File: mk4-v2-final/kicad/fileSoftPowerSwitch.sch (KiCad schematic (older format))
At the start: 11 parts, among them Q20 Q_NMOS_GDS, Q21 2N3904, Q22 2N3904

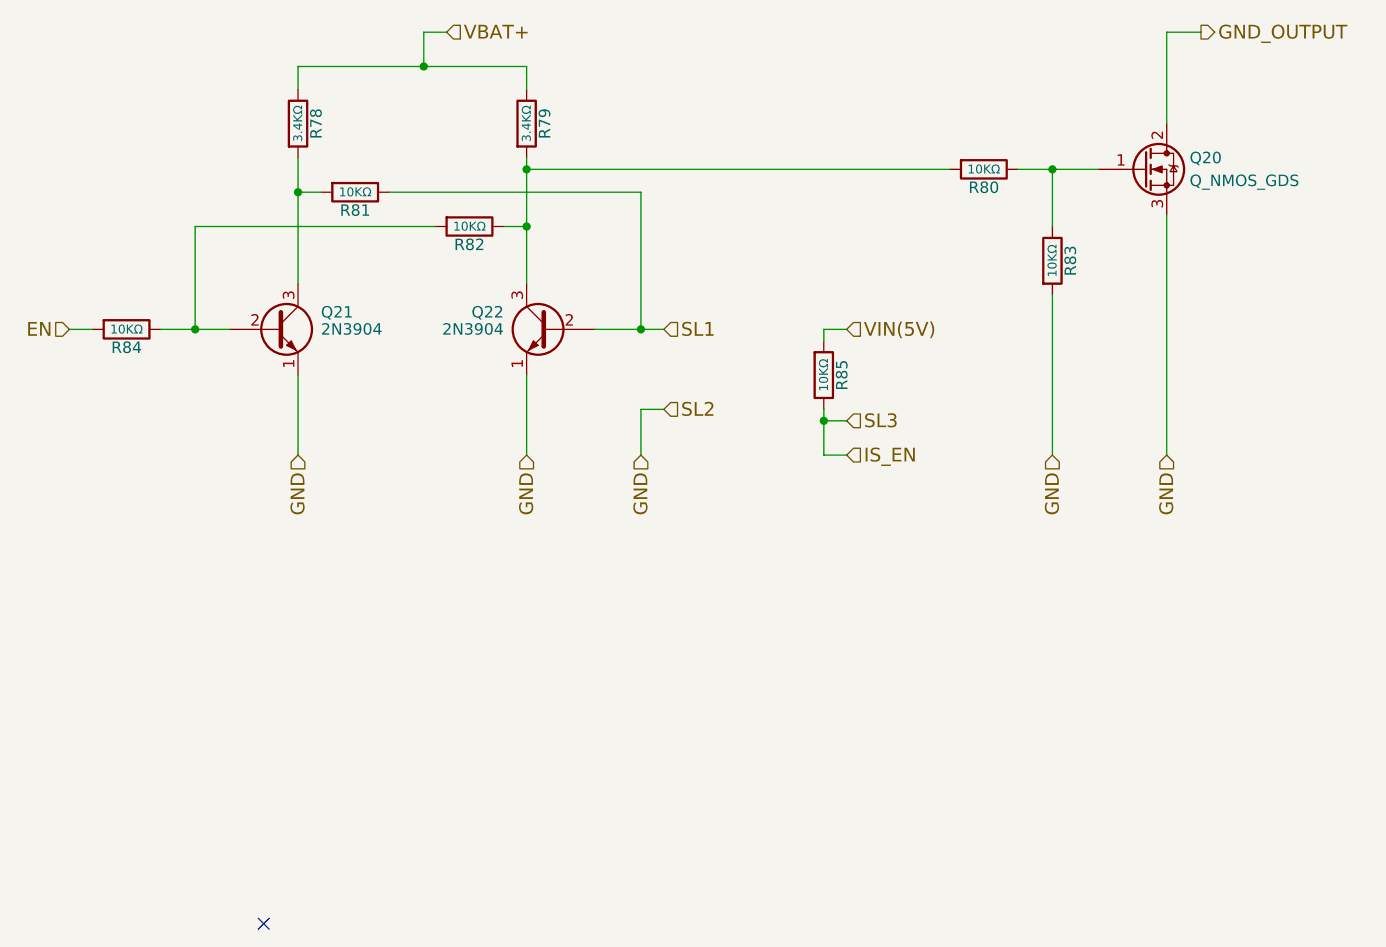
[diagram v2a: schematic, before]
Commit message: schematic is done, footprint association and netlist are also done
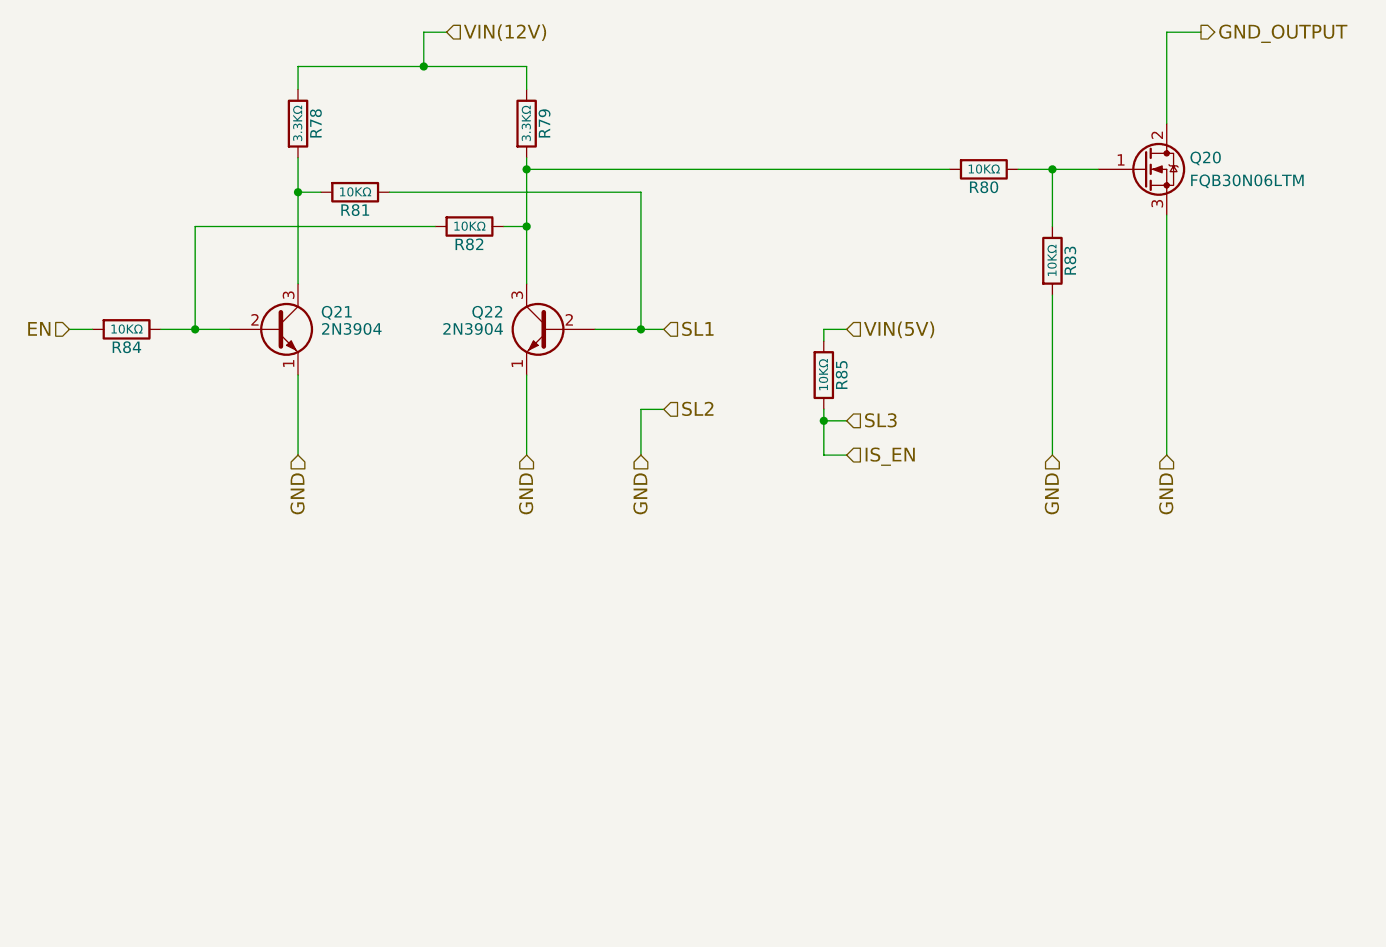
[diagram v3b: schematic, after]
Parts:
- Q20: value Q_NMOS_GDS -> FQB30N06LTM; footprint TO_SOT_Packages_THT:TO-220-3_Vertical -> TO_SOT_Packages_SMD:TO-263-3_TabPin2; digikey-pn (none) -> FQB30N06LTMCT-ND; mfg-pn (none) -> FQB30N06LTM
- Q21, Q22: digikey-pn (none) -> 2N3904FS-ND; mfg-pn (none) -> 2N3904BU
- R78, R79: value 3.4KΩ -> 3.3KΩ; footprint Resistors_THT:R_Axial_DIN0207_L6.3mm_D2.5mm_P10.16mm_Horizontal -> Resistors_THT:R_Axial_DIN0204_L3.6mm_D1.6mm_P5.08mm_Horizontal; digikey-pn (none) -> BC3499CT-ND; mfg-pn (none) -> MBA02040C3301FRP00
- R80, R81, R82, R83, R84, R85: footprint Resistors_THT:R_Axial_DIN0207_L6.3mm_D2.5mm_P10.16mm_Horizontal -> Resistors_THT:R_Axial_DIN0204_L3.6mm_D1.6mm_P5.08mm_Horizontal; digikey-pn (none) -> BC10.0KXCT-ND; mfg-pn (none) -> MBA02040C1002FRP00
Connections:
- net VBAT+ renamed VIN(12V)
- no-connect marks 1 -> 0
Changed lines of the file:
@@
 EESchema Schematic File Version 2
-LIBS:hitchco-mk4-rescue
 LIBS:power
 LIBS:device
@@
 LIBS:cd4013b
 LIBS:ncs3s1205sc
+LIBS:lca715
+LIBS:SN74HC595N
+LIBS:CD74HC4067
 LIBS:hitchco-mk4-cache
 EELAYER 25 0
@@
 $Descr A4 11693 8268
 encoding utf-8
-Sheet 44 54
+Sheet 40 54
 Title ""
 Date ""
@@
 P 4400 2750
 F 0 "R78" V 4480 2750 50  0000 C CNN
-F 1 "3.4KΩ" V 4400 2750 39  0000 C CNN
-F 2 "Resistors_THT:R_Axial_DIN0207_L6.3mm_D2.5mm_P10.16mm_Horizontal" V 4330 2750 50  0001 C CNN
+F 1 "3.3KΩ" V 4400 2750 39  0000 C CNN
+F 2 "Resistors_THT:R_Axial_DIN0204_L3.6mm_D1.6mm_P5.08mm_Horizontal" V 4330 2750 50  0001 C CNN
 F 3 "" H 4400 2750 50  0001 C CNN
+F 4 "BC3499CT-ND" H 4480 2850 50  0001 C CNN "digikey-pn"
+F 5 "MBA02040C3301FRP00" H 4480 2850 50  0001 C CNN "mfg-pn"
 	1    4400 2750
 	1    0    0    -1
@@
 F 0 "R81" V 4730 3050 50  0000 C CNN
 F 1 "10KΩ" V 4650 3050 39  0000 C CNN
-F 2 "Resistors_THT:R_Axial_DIN0207_L6.3mm_D2.5mm_P10.16mm_Horizontal" V 4580 3050 50  0001 C CNN
+F 2 "Resistors_THT:R_Axial_DIN0204_L3.6mm_D1.6mm_P5.08mm_Horizontal" V 4580 3050 50  0001 C CNN
 F 3 "" H 4650 3050 50  0001 C CNN
+F 4 "BC10.0KXCT-ND" H 4730 3150 50  0001 C CNN "digikey-pn"
+F 5 "MBA02040C1002FRP00" H 4730 3150 50  0001 C CNN "mfg-pn"
 	1    4650 3050
 	0    1    1    0
@@
 F 1 "2N3904" H 4500 3650 50  0000 L CNN
 F 2 "TO_SOT_Packages_THT:TO-92_Molded_Narrow" H 4500 3575 50  0001 L CIN
-F 3 "" H 4300 3650 50  0001 L CNN
+F 3 "https://www.fairchildsemi.com/datasheets/MM/MMBT3904.pdf" H 4300 3650 50  0001 L CNN
+F 4 "2N3904FS-ND" H 4500 3825 50  0001 C CNN "digikey-pn"
+F 5 "2N3904BU" H 4500 3825 50  0001 C CNN "mfg-pn"
 	1    4300 3650
 	1    0    0    -1
@@
 F 0 "R82" V 5230 3200 50  0000 C CNN
 F 1 "10KΩ" V 5150 3200 39  0000 C CNN
-F 2 "Resistors_THT:R_Axial_DIN0207_L6.3mm_D2.5mm_P10.16mm_Horizontal" V 5080 3200 50  0001 C CNN
+F 2 "Resistors_THT:R_Axial_DIN0204_L3.6mm_D1.6mm_P5.08mm_Horizontal" V 5080 3200 50  0001 C CNN
 F 3 "" H 5150 3200 50  0001 C CNN
+F 4 "BC10.0KXCT-ND" H 5230 3300 50  0001 C CNN "digikey-pn"
+F 5 "MBA02040C1002FRP00" H 5230 3300 50  0001 C CNN "mfg-pn"
 	1    5150 3200
 	0    1    1    0
@@
 P 5400 2750
 F 0 "R79" V 5480 2750 50  0000 C CNN
-F 1 "3.4KΩ" V 5400 2750 39  0000 C CNN
-F 2 "Resistors_THT:R_Axial_DIN0207_L6.3mm_D2.5mm_P10.16mm_Horizontal" V 5330 2750 50  0001 C CNN
+F 1 "3.3KΩ" V 5400 2750 39  0000 C CNN
+F 2 "Resistors_THT:R_Axial_DIN0204_L3.6mm_D1.6mm_P5.08mm_Horizontal" V 5330 2750 50  0001 C CNN
 F 3 "" H 5400 2750 50  0001 C CNN
+F 4 "BC3499CT-ND" H 5480 2850 50  0001 C CNN "digikey-pn"
+F 5 "MBA02040C3301FRP00" H 5480 2850 50  0001 C CNN "mfg-pn"
 	1    5400 2750
 	1    0    0    -1
@@
 F 1 "2N3904" H 5700 3650 50  0000 L CNN
 F 2 "TO_SOT_Packages_THT:TO-92_Molded_Narrow" H 5700 3575 50  0001 L CIN
-F 3 "" H 5500 3650 50  0001 L CNN
+F 3 "https://www.fairchildsemi.com/datasheets/MM/MMBT3904.pdf" H 5500 3650 50  0001 L CNN
+F 4 "2N3904FS-ND" H 5700 3825 50  0001 C CNN "digikey-pn"
+F 5 "2N3904BU" H 5700 3825 50  0001 C CNN "mfg-pn"
 	1    5500 3650
 	-1   0    0    -1
 $EndComp
-Text HLabel 5400 4200 3    60   Input ~ 0
-GND
-Text HLabel 4400 4200 3    60   Input ~ 0
-GND
-Text HLabel 5050 2350 2    60   Input ~ 0
-VBAT+
 $Comp
 L R R80
@@
 F 0 "R80" V 7480 2950 50  0000 C CNN
 F 1 "10KΩ" V 7400 2950 39  0000 C CNN
-F 2 "Resistors_THT:R_Axial_DIN0207_L6.3mm_D2.5mm_P10.16mm_Horizontal" V 7330 2950 50  0001 C CNN
+F 2 "Resistors_THT:R_Axial_DIN0204_L3.6mm_D1.6mm_P5.08mm_Horizontal" V 7330 2950 50  0001 C CNN
 F 3 "" H 7400 2950 50  0001 C CNN
+F 4 "BC10.0KXCT-ND" H 7480 3050 50  0001 C CNN "digikey-pn"
+F 5 "MBA02040C1002FRP00" H 7480 3050 50  0001 C CNN "mfg-pn"
 	1    7400 2950
 	0    1    1    0
@@
 F 0 "R83" V 7780 3350 50  0000 C CNN
 F 1 "10KΩ" V 7700 3350 39  0000 C CNN
-F 2 "Resistors_THT:R_Axial_DIN0207_L6.3mm_D2.5mm_P10.16mm_Horizontal" V 7630 3350 50  0001 C CNN
+F 2 "Resistors_THT:R_Axial_DIN0204_L3.6mm_D1.6mm_P5.08mm_Horizontal" V 7630 3350 50  0001 C CNN
 F 3 "" H 7700 3350 50  0001 C CNN
+F 4 "BC10.0KXCT-ND" H 7780 3450 50  0001 C CNN "digikey-pn"
+F 5 "MBA02040C1002FRP00" H 7780 3450 50  0001 C CNN "mfg-pn"
 	1    7700 3350
 	1    0    0    -1
 $EndComp
+$Comp
+L R R85
+U 1 1 5A25E32E
+P 6700 3850
+F 0 "R85" V 6780 3850 50  0000 C CNN
+F 1 "10KΩ" V 6700 3850 39  0000 C CNN
+F 2 "Resistors_THT:R_Axial_DIN0204_L3.6mm_D1.6mm_P5.08mm_Horizontal" V 6630 3850 50  0001 C CNN
+F 3 "" H 6700 3850 50  0001 C CNN
+F 4 "BC10.0KXCT-ND" H 6780 3950 50  0001 C CNN "digikey-pn"
+F 5 "MBA02040C1002FRP00" H 6780 3950 50  0001 C CNN "mfg-pn"
+	1    6700 3850
+	1    0    0    1
+$EndComp
+$Comp
+L R R84
+U 1 1 5A25E339
+P 3650 3650
+F 0 "R84" V 3730 3650 50  0000 C CNN
+F 1 "10KΩ" V 3650 3650 39  0000 C CNN
+F 2 "Resistors_THT:R_Axial_DIN0204_L3.6mm_D1.6mm_P5.08mm_Horizontal" V 3580 3650 50  0001 C CNN
+F 3 "" H 3650 3650 50  0001 C CNN
+F 4 "BC10.0KXCT-ND" H 3730 3750 50  0001 C CNN "digikey-pn"
+F 5 "MBA02040C1002FRP00" H 3730 3750 50  0001 C CNN "mfg-pn"
+	1    3650 3650
+	0    1    1    0
+$EndComp
+$Comp
+L Q_NMOS_GDS Q20
+U 1 1 5A2EEE12
+P 8100 2950
+F 0 "Q20" H 8300 3000 50  0000 L CNN
+F 1 "FQB30N06LTM" H 8300 2900 50  0000 L CNN
+F 2 "TO_SOT_Packages_SMD:TO-263-3_TabPin2" H 8300 3050 50  0001 C CNN
+F 3 "http://www.onsemi.com/pub/Collateral/NTB5605P-D.PDF" H 8100 2950 50  0001 C CNN
+F 4 "FQB30N06LTMCT-ND" H 8300 3100 50  0001 C CNN "digikey-pn"
+F 5 "FQB30N06LTM" H 8300 3100 50  0001 C CNN "mfg-pn"
+	1    8100 2950
+	1    0    0    -1
+$EndComp
+Text HLabel 5400 4200 3    60   Input ~ 0
+GND
+Text HLabel 4400 4200 3    60   Input ~ 0
+GND
 Text HLabel 7700 4200 3    60   Input ~ 0
 GND
@@
 Text HLabel 6800 4050 2    60   Input ~ 0
 SL3
-$Comp
-L R R85
-U 1 1 5A25E32E
-P 6700 3850
-F 0 "R85" V 6780 3850 50  0000 C CNN
-F 1 "10KΩ" V 6700 3850 39  0000 C CNN
-F 2 "Resistors_THT:R_Axial_DIN0207_L6.3mm_D2.5mm_P10.16mm_Horizontal" V 6630 3850 50  0001 C CNN
-F 3 "" H 6700 3850 50  0001 C CNN
-	1    6700 3850
-	1    0    0    1
-$EndComp
 Text HLabel 6800 3650 2    60   Input ~ 0
 VIN(5V)
-$Comp
-L R R84
-U 1 1 5A25E339
-P 3650 3650
-F 0 "R84" V 3730 3650 50  0000 C CNN
-F 1 "10KΩ" V 3650 3650 39  0000 C CNN
-F 2 "Resistors_THT:R_Axial_DIN0207_L6.3mm_D2.5mm_P10.16mm_Horizontal" V 3580 3650 50  0001 C CNN
-F 3 "" H 3650 3650 50  0001 C CNN
-	1    3650 3650
-	0    1    1    0
-$EndComp
-Wire Wire Line
-	4400 2900 4400 3450
-Wire Wire Line
-	5400 2900 5400 3450
-Wire Wire Line
-	3950 3200 3950 3650
-Connection ~ 5400 3200
-Wire Wire Line
-	5000 3200 3950 3200
-Wire Wire Line
-	5300 3200 5400 3200
-Wire Wire Line
-	5400 3850 5400 4200
-Wire Wire Line
-	4400 3850 4400 4200
-Connection ~ 3950 3650
-Wire Wire Line
-	4400 2600 4400 2500
-Wire Wire Line
-	4400 2500 5400 2500
-Wire Wire Line
-	4950 2350 4950 2500
-Wire Wire Line
-	5400 2500 5400 2600
-Connection ~ 4950 2500
-Wire Wire Line
-	5400 2950 7250 2950
-Connection ~ 5400 2950
-Wire Wire Line
-	7700 3200 7700 2950
-Wire Wire Line
-	7700 3500 7700 4200
-Wire Wire Line
-	8200 3150 8200 4200
-Wire Wire Line
-	8200 2350 8200 2750
-Wire Wire Line
-	5700 3650 6000 3650
-Connection ~ 5900 3650
-Connection ~ 4400 3050
-Wire Wire Line
-	4400 3050 4500 3050
-Wire Wire Line
-	4800 3050 5900 3050
-Connection ~ 7700 2950
-Wire Wire Line
-	5900 3050 5900 3650
-Wire Wire Line
-	6800 4050 6700 4050
-Wire Wire Line
-	6700 4000 6700 4200
-Wire Wire Line
-	6800 3650 6700 3650
-Wire Wire Line
-	6700 3650 6700 3700
-Wire Wire Line
-	6000 4000 5900 4000
-Wire Wire Line
-	5900 4000 5900 4200
-Wire Wire Line
-	6700 4200 6800 4200
-Connection ~ 6700 4050
-Wire Wire Line
-	7550 2950 7900 2950
-Wire Wire Line
-	8350 2350 8200 2350
-Wire Wire Line
-	4950 2350 5050 2350
 Text HLabel 6800 4200 2    60   Input ~ 0
 IS_EN
 Text HLabel 3400 3650 0    60   Input ~ 0
 EN
-NoConn ~ 4250 6250
-$Comp
-L Q_NMOS_GDS Q20
-U 1 1 5A2EEE12
-P 8100 2950
-F 0 "Q20" H 8300 3000 50  0000 L CNN
-F 1 "Q_NMOS_GDS" H 8300 2900 50  0000 L CNN
-F 2 "TO_SOT_Packages_THT:TO-220-3_Vertical" H 8300 3050 50  0001 C CNN
-F 3 "" H 8100 2950 50  0001 C CNN
-	1    8100 2950
-	1    0    0    -1
-$EndComp
+Text HLabel 5050 2350 2    60   Input ~ 0
+VIN(12V)
+Wire Wire Line
+	4400 2900 4400 3450
+Wire Wire Line
+	5400 2900 5400 3450
+Wire Wire Line
+	3950 3200 3950 3650
+Wire Wire Line
+	5000 3200 3950 3200
+Wire Wire Line
+	5300 3200 5400 3200
+Wire Wire Line
+	5400 3850 5400 4200
+Wire Wire Line
+	4400 3850 4400 4200
+Wire Wire Line
+	4400 2600 4400 2500
+Wire Wire Line
+	4400 2500 5400 2500
+Wire Wire Line
+	4950 2350 4950 2500
+Wire Wire Line
+	5400 2500 5400 2600
+Wire Wire Line
+	5400 2950 7250 2950
+Wire Wire Line
+	7700 3200 7700 2950
+Wire Wire Line
+	7700 3500 7700 4200
+Wire Wire Line
+	8200 3150 8200 4200
+Wire Wire Line
+	8200 2350 8200 2750
+Wire Wire Line
+	5700 3650 6000 3650
+Wire Wire Line
+	4400 3050 4500 3050
+Wire Wire Line
+	4800 3050 5900 3050
+Wire Wire Line
+	5900 3050 5900 3650
+Wire Wire Line
+	6800 4050 6700 4050
+Wire Wire Line
+	6700 4000 6700 4200
+Wire Wire Line
+	6800 3650 6700 3650
+Wire Wire Line
+	6700 3650 6700 3700
+Wire Wire Line
+	6000 4000 5900 4000
+Wire Wire Line
+	5900 4000 5900 4200
+Wire Wire Line
+	6700 4200 6800 4200
+Wire Wire Line
+	7550 2950 7900 2950
+Wire Wire Line
+	8350 2350 8200 2350
+Wire Wire Line
+	4950 2350 5050 2350
 Wire Wire Line
 	3400 3650 3500 3650
 Wire Wire Line
 	3800 3650 4100 3650
+Connection ~ 5400 3200
+Connection ~ 3950 3650
+Connection ~ 4950 2500
+Connection ~ 5400 2950
+Connection ~ 5900 3650
+Connection ~ 4400 3050
+Connection ~ 7700 2950
+Connection ~ 6700 4050
 $EndSCHEMATC

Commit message: all components on the board
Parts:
- Q21, Q22: footprint TO_SOT_Packages_THT:TO-92_Molded_Narrow -> TO_SOT_Packages_THT:TO-92_Inline_Narrow_Oval
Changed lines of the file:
@@
 F 0 "Q21" H 4500 3725 50  0000 L CNN
 F 1 "2N3904" H 4500 3650 50  0000 L CNN
-F 2 "TO_SOT_Packages_THT:TO-92_Molded_Narrow" H 4500 3575 50  0001 L CIN
+F 2 "TO_SOT_Packages_THT:TO-92_Inline_Narrow_Oval" H 4500 3575 50  0001 L CIN
 F 3 "https://www.fairchildsemi.com/datasheets/MM/MMBT3904.pdf" H 4300 3650 50  0001 L CNN
 F 4 "2N3904FS-ND" H 4500 3825 50  0001 C CNN "digikey-pn"
@@
 F 0 "Q22" H 5700 3725 50  0000 L CNN
 F 1 "2N3904" H 5700 3650 50  0000 L CNN
-F 2 "TO_SOT_Packages_THT:TO-92_Molded_Narrow" H 5700 3575 50  0001 L CIN
+F 2 "TO_SOT_Packages_THT:TO-92_Inline_Narrow_Oval" H 5700 3575 50  0001 L CIN
 F 3 "https://www.fairchildsemi.com/datasheets/MM/MMBT3904.pdf" H 5500 3650 50  0001 L CNN
 F 4 "2N3904FS-ND" H 5700 3825 50  0001 C CNN "digikey-pn"
